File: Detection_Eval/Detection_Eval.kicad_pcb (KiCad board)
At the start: 2 copper layers, 6 parts

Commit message: Madison_01-20_2
Updated further footprints
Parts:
- added U4: ~, Detection_Eval_lib_fp:DIALIGHT_3LED, F.Cu at (50.3, 151.8)

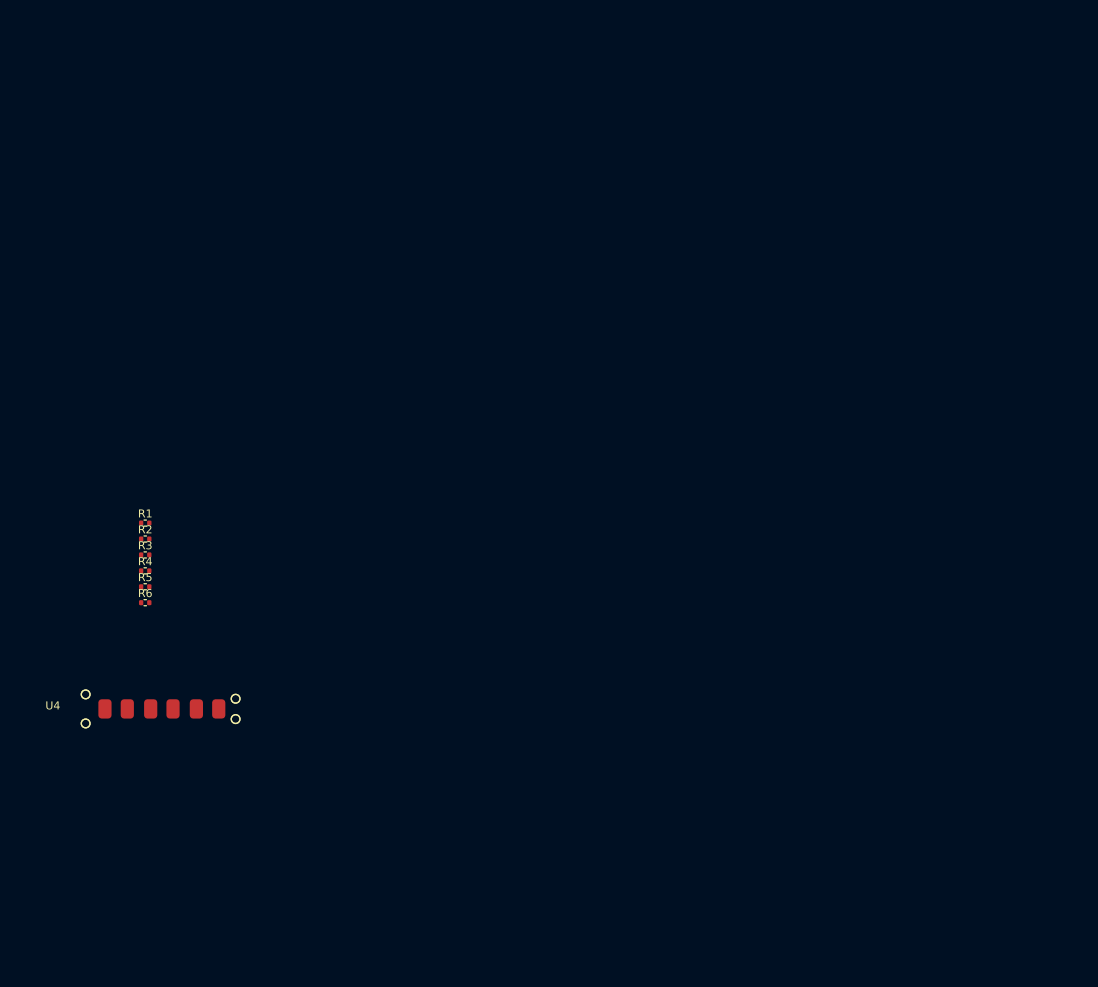
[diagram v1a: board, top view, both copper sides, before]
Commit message: Madison_02-05_2
Added battery charger circuit
Added footprints to accelerometer, lcd screen, buttons, AND gate, batt charger, batt holder
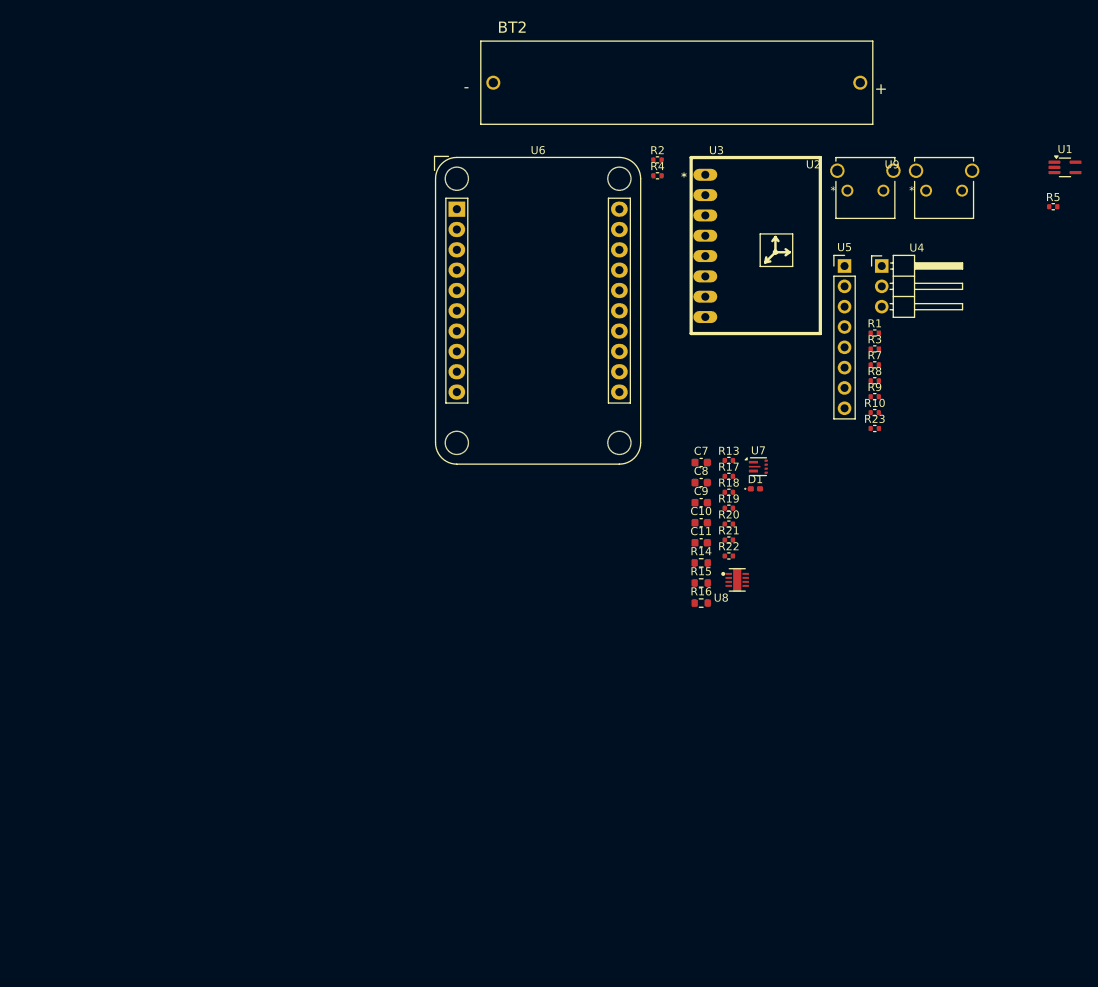
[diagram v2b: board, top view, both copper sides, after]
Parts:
- removed R6: 10k, Resistor_SMD:R_0402_1005Metric
- added BT2: BH-18650-PC, Detection_Eval_lib_fp:BAT_BEAAAAPC, F.Cu at (124.2, 73.5)
- added C10: 1uF, Capacitor_SMD:C_0603_1608Metric, F.Cu at (127.2, 128.5)
- added C11: 100nF, Capacitor_SMD:C_0603_1608Metric, F.Cu at (127.2, 131.0)
- added C7: 1uF, Capacitor_SMD:C_0603_1608Metric, F.Cu at (127.2, 121.0)
- added C8: 10uF, Capacitor_SMD:C_0603_1608Metric, F.Cu at (127.2, 123.5)
- added C9: 1uF, Capacitor_SMD:C_0603_1608Metric, F.Cu at (127.2, 126.0)
- added D1: LED, LED_SMD:LED_0402_1005Metric_Pad0.77x0.64mm_HandSolder, F.Cu at (134.0, 124.3)
- added R10: 430, Resistor_SMD:R_0402_1005Metric, F.Cu at (148.9, 114.7)
- added R13: 10k, Resistor_SMD:R_0402_1005Metric, F.Cu at (130.7, 120.7)
- added R14: 5.1k, Resistor_SMD:R_0603_1608Metric, F.Cu at (127.2, 133.5)
- added R15: 5.1k, Resistor_SMD:R_0603_1608Metric, F.Cu at (127.2, 136.0)
- added R16: 100k, Resistor_SMD:R_0603_1608Metric, F.Cu at (127.2, 138.5)
- added R17: 0, Resistor_SMD:R_0402_1005Metric, F.Cu at (130.7, 122.7)
- added R18: 0, Resistor_SMD:R_0402_1005Metric, F.Cu at (130.7, 124.7)
- added R19: 10k, Resistor_SMD:R_0402_1005Metric, F.Cu at (130.7, 126.7)
- added R20: 3k, Resistor_SMD:R_0402_1005Metric, F.Cu at (130.7, 128.7)
- added R21: 62k, Resistor_SMD:R_0402_1005Metric, F.Cu at (130.7, 130.7)
- added R22: 36k, Resistor_SMD:R_0402_1005Metric, F.Cu at (130.7, 132.7)
- added R23: 0, Resistor_SMD:R_0402_1005Metric, F.Cu at (148.9, 116.7)
- added R7: 1k, Resistor_SMD:R_0402_1005Metric, F.Cu at (148.9, 108.8)
- added R8: 10k, Resistor_SMD:R_0402_1005Metric, F.Cu at (148.9, 110.8)
- added R9: 1k, Resistor_SMD:R_0402_1005Metric, F.Cu at (148.9, 112.7)
- added U1: SN74LVC1G08DCKR, Package_TO_SOT_SMD:SOT-353_SC-70-5_Handsoldering, F.Cu at (172.7, 84.1)
- added U2: ~, Detection_Eval_lib_fp:SW2_1825027-C_TEC, F.Cu at (145.5, 87.0)
- added U3: ~, Detection_Eval_lib_fp:GY-521, F.Cu at (126.0, 104.9)
- added U5: ~, Connector_PinHeader_2.54mm:PinHeader_1x08_P2.54mm_Vertical, F.Cu at (145.2, 96.4)
- added U6: ESP8266, Module:Adafruit_HUZZAH_ESP8266_breakout_WithMountingHoles, F.Cu at (96.7, 89.3)
- added U7: TPS61022, Package_DFN_QFN:Texas_RWU0007A_VQFN-7_2x2mm_P0.5mm, F.Cu at (134.4, 121.5)
- added U8: ~, Detection_Eval_lib_fp:BQ25172DSGR, F.Cu at (131.7, 135.7)
- added U9: ~, Detection_Eval_lib_fp:SW2_1825027-C_TEC, F.Cu at (155.3, 87.0)
- R1, R2: value 10k -> 0
- R3: value 220 -> 10k
- R4: value 220 -> 0
- R5: value 220 -> 1k
- U4: footprint Detection_Eval_lib_fp:DIALIGHT_3LED -> Connector_PinHeader_2.54mm:PinHeader_1x03_P2.54mm_Horizontal
- moved R5 123.0 mm to (171.2, 89.0)
- moved U4 113.9 mm to (149.8, 96.4)
- moved R3 94.8 mm to (148.9, 106.8)
- moved R1 94.2 mm to (148.9, 104.8)
- moved R4 80.9 mm to (121.8, 85.1)
- moved R2 79.7 mm to (121.8, 83.1)
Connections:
- R1 pad 1: BUTTON1 -> Net-(C1-Pad2)
- R1 pad 2: GND -> /BUTTON1
- R2 pad 1: BUTTON2 -> +5V
- R2 pad 2: GND -> Net-(U6-VIN)
- R3 pad 1: GREEN_PGOOD -> Net-(C1-Pad2)
- R3 pad 2: Net-(R3-Pad2) -> GND
- R4 pad 1: RED_ALERT -> +5V
- R4 pad 2: Net-(R4-Pad2) -> Net-(U6-VBAT)
- R5 pad 1: YELLOW_STAT -> FAILSAFE
- R5 pad 2: Net-(R5-Pad2) -> Net-(U6-GPIO12)
- U4 pad 1: GND -> Net-(U4-SIGNAL)
- U4 pad 2: Net-(R3-Pad2) -> +3V3

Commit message: Madison_02-06
final footprints added and layout positioning mostly done
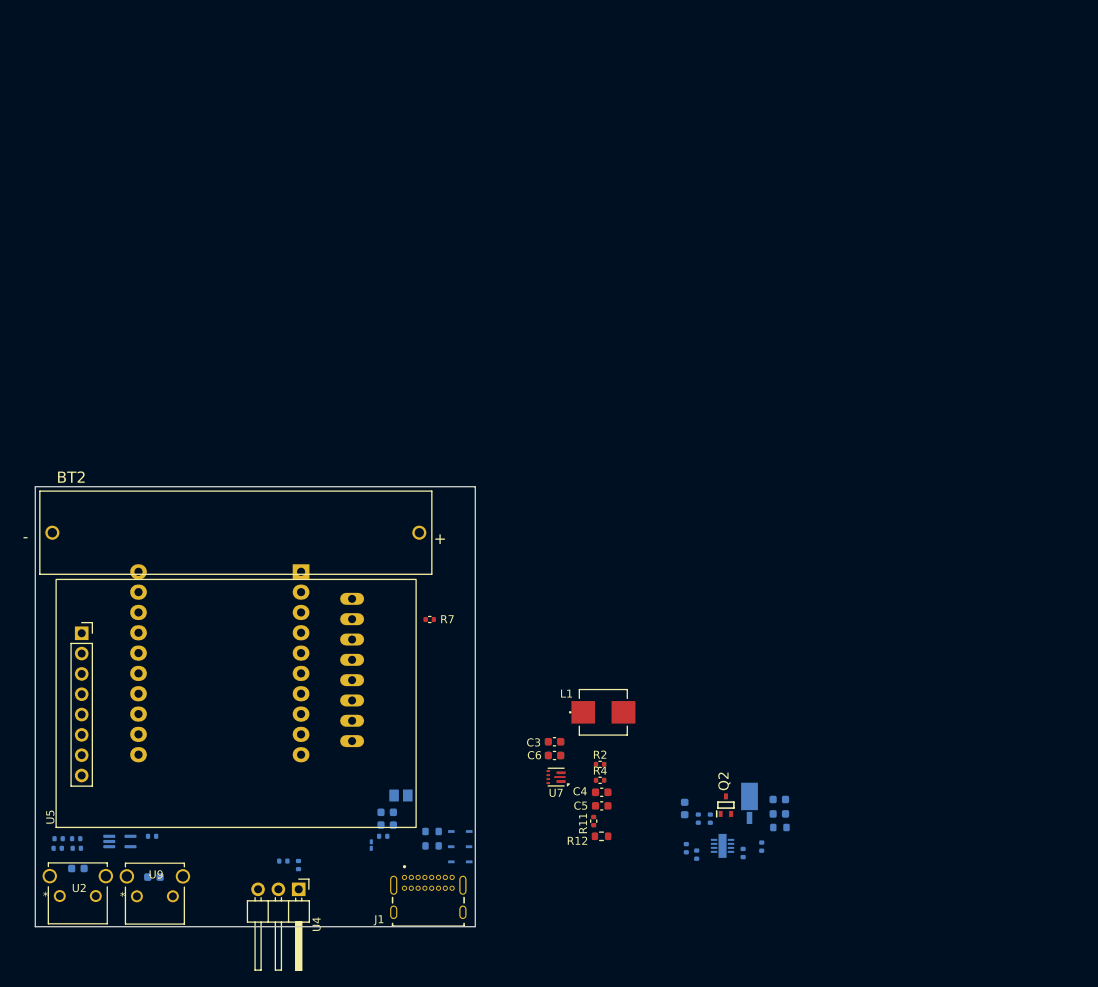
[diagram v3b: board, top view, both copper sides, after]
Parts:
- added C1: 0.1u, Capacitor_SMD:C_0603_1608Metric, B.Cu at (58.8, 172.8)
- added C2: 0.1u, Capacitor_SMD:C_0603_1608Metric, B.Cu at (49.3, 171.7)
- added C3: 10u, Capacitor_SMD:C_0603_1608Metric, F.Cu at (108.9, 155.9)
- added C4: 47u, Capacitor_SMD:C_0603_1608Metric, F.Cu at (114.8, 162.2)
- added C5: 47u, Capacitor_SMD:C_0603_1608Metric, F.Cu at (114.8, 163.9)
- added C6: 10u, Capacitor_SMD:C_0603_1608Metric, F.Cu at (108.9, 157.6)
- added D2: UPS115UE3/TR7, Footprints:POWERMITE1_DO-216AA_MIS_MCH, B.Cu at (133.3, 163.2)
- added D4: TSD05CDYFR, Footprints:TVS_SOD2_DYF_TEX-L, B.Cu at (97.1, 170.9)
- added D5: TSD05CDYFR, Footprints:TVS_SOD2_DYF_TEX-L, B.Cu at (97.1, 169.0)
- added D6: TSD05CDYFR, Footprints:TVS_SOD2_DYF_TEX-L, B.Cu at (97.1, 167.1)
- added FB1: FBMJ2125HS250NT, Footprints:BEADC2012X105N, B.Cu at (89.7, 162.6)
- added J1: USB4085-GF-A_REVB, Footprints:GCT_USB4085-GF-A_REVB, F.Cu at (93.1, 177.2)
- added L1: 1u, Detection_Eval_lib_fp:IND_IHLP-2020CZ, F.Cu at (115.0, 152.2)
- added Q2: PMOS, Footprints:SOT65P210X110-3N, F.Cu at (130.3, 163.8)
- added R11: 732K, Resistor_SMD:R_0402_1005Metric, F.Cu at (113.8, 165.8)
- added R12: 100K, Resistor_SMD:R_0603_1608Metric, F.Cu at (114.8, 167.7)
- C10, C11, C7, C8, C9, R1, R10, R13, R14, R15, R16, R17, R18, R19, R20, R21, R22, R23, R3, R8, R9, U1, U3, U8: moved to B.Cu
- D1: value LED -> 150060YS75000; footprint LED_SMD:LED_0402_1005Metric_Pad0.77x0.64mm_HandSolder -> LED_SMD:LED_0201_0603Metric_Pad0.64x0.40mm_HandSolder; moved to B.Cu
- R5: value 1k -> 10k; moved to B.Cu
- U5: footprint Connector_PinHeader_2.54mm:PinHeader_1x08_P2.54mm_Vertical -> Detection_Eval_lib_fp:LCDSCREEN
- U6: footprint Module:Adafruit_HUZZAH_ESP8266_breakout_WithMountingHoles -> Module:Adafruit_HUZZAH_ESP8266_breakout; moved to B.Cu
- moved U1 145.1 mm to (54.6, 168.3)
- moved R5 137.4 mm to (58.6, 167.7)
- moved U9 132.3 mm to (56.7, 175.2)
- moved U2 132.2 mm to (47.1, 175.2)
- moved U5 121.0 mm to (46.6, 166.6), turned to 90 degrees
- moved R3 119.7 mm to (46.8, 169.2), turned to 180 degrees
- moved R1 118.7 mm to (49.2, 169.2)
- moved R8 117.0 mm to (46.9, 168.0), turned to 180 degrees
- moved R23 112.2 mm to (49.1, 168.0)
- moved U4 106.7 mm to (76.9, 174.3), turned to -90 degrees
- moved R9 92.8 mm to (76.9, 171.3), turned to 90 degrees
- moved R10 92.8 mm to (75.0, 170.8), turned to 180 degrees
- moved BT2 78.8 mm to (69.1, 129.8)
- moved R2 75.9 mm to (114.6, 158.7)
- moved R4 75.9 mm to (114.6, 160.7)
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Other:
- board outline added: 55 x 55 mm

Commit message: LAYOUT DONE
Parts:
- C3, C6, L1, Q2, R7, U7: moved to B.Cu
- D1: moved to F.Cu
- moved C6 74.9 mm to (141.0, 89.9), turned to 90 degrees
- moved C3 74.1 mm to (142.7, 89.9), turned to 90 degrees
- moved U7 72.7 mm to (141.9, 95.5), turned to 0 degrees
- moved R16 68.4 mm to (131.0, 98.5), turned to 180 degrees
- moved R12 68.1 mm to (142.1, 105.3), turned to -90 degrees
- moved R11 67.0 mm to (143.4, 105.7), turned to 90 degrees
- moved C9 66.0 mm to (143.3, 100.7)
- moved R18 65.9 mm to (141.5, 101.3), turned to -90 degrees
- moved R21 65.7 mm to (130.2, 103.7), turned to 0 degrees
- moved R17 65.3 mm to (140.1, 101.3), turned to 90 degrees
- moved R20 65.1 mm to (139.3, 104.0), turned to 180 degrees
- moved U8 65.0 mm to (135.6, 104.1)
- moved R22 65.0 mm to (130.2, 105.1), turned to 0 degrees
- moved C7 64.9 mm to (131.1, 100.3), turned to 180 degrees
- moved R19 64.9 mm to (139.3, 105.3), turned to 180 degrees
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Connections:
- C1 pad 1: +BATT -> +5V
- C2 pad 1: +BATT -> +5V
- C3 pad 1: +VCC -> VCC
- C6 pad 1: +VCC -> VCC
- L1 pad 1: +VCC -> VCC
- U1 pad 5: +BATT -> +5V
- U2 pad 2: +BATT -> +5V
- U7 pad 5: +VCC -> VCC
- U7 pad 7: +VCC -> VCC
- U9 pad 2: +BATT -> +5V
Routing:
- net RESET: track 0.00 -> 61.1 mm
- net HSPI_MOSI: track 0.00 -> 54.9 mm
- net HSPI_CLK: track 0.00 -> 53.9 mm
- net SCL_ACCEL: track 0.00 -> 53.2 mm
- net SDA_ACCEL: track 0.00 -> 45.4 mm
- net ECG: track 0.00 -> 34.0 mm, vias 0 -> 1
- net Net-(U6-GPIO12): track 0.00 -> 33.1 mm, vias 0 -> 1
- net Net-(D1-K): track 0.00 -> 31.3 mm, vias 0 -> 1
- net BACKLIGHT: track 0.00 -> 25.5 mm
- net Net-(U6-VBAT): track 0.00 -> 24.0 mm, vias 0 -> 1
- net Net-(U6-VIN): track 0.00 -> 23.4 mm, vias 0 -> 1
- net /Battery/CC2: track 0.00 -> 22.9 mm, vias 0 -> 1
- net Net-(C1-Pad2): track 0.00 -> 17.2 mm
- net FAILSAFE: track 0.00 -> 17.1 mm, vias 0 -> 2
- net GND: track 0.00 -> 16.7 mm, vias 0 -> 32
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- added copper zone on In2.Cu, net +3V3
- added copper zone on B.Cu, net +5V
- added copper zone on F.Cu, net +5V
- added copper zone on In2.Cu, net +5V
- added copper zone on B.Cu, net GND
- added copper zone on F.Cu, net GND
- added copper zone on In1.Cu, net GND
- added copper zone on B.Cu, net Net-(BT2-PadP)
- added copper zone on F.Cu, net Net-(BT2-PadP)
- added copper zone on B.Cu, net Net-(U7-SW)
- added copper zone on B.Cu, net VBUS
- added copper zone on B.Cu, net VCC
- added copper zone on In2.Cu, net VCC
- added copper zone on B.Cu, net VDD
- added copper zone on In2.Cu, net VDD
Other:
- copper layers 2 -> 4
